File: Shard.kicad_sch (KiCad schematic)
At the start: 27 parts, among them J1 USB_C_Receptacle_USB2.0_16P, J2 Conn_01x02_Pin, U1 ESP32-S3, U2 USBLC6-2P6, U3 TLV76733DRVx, U4 TLV76733DRVx

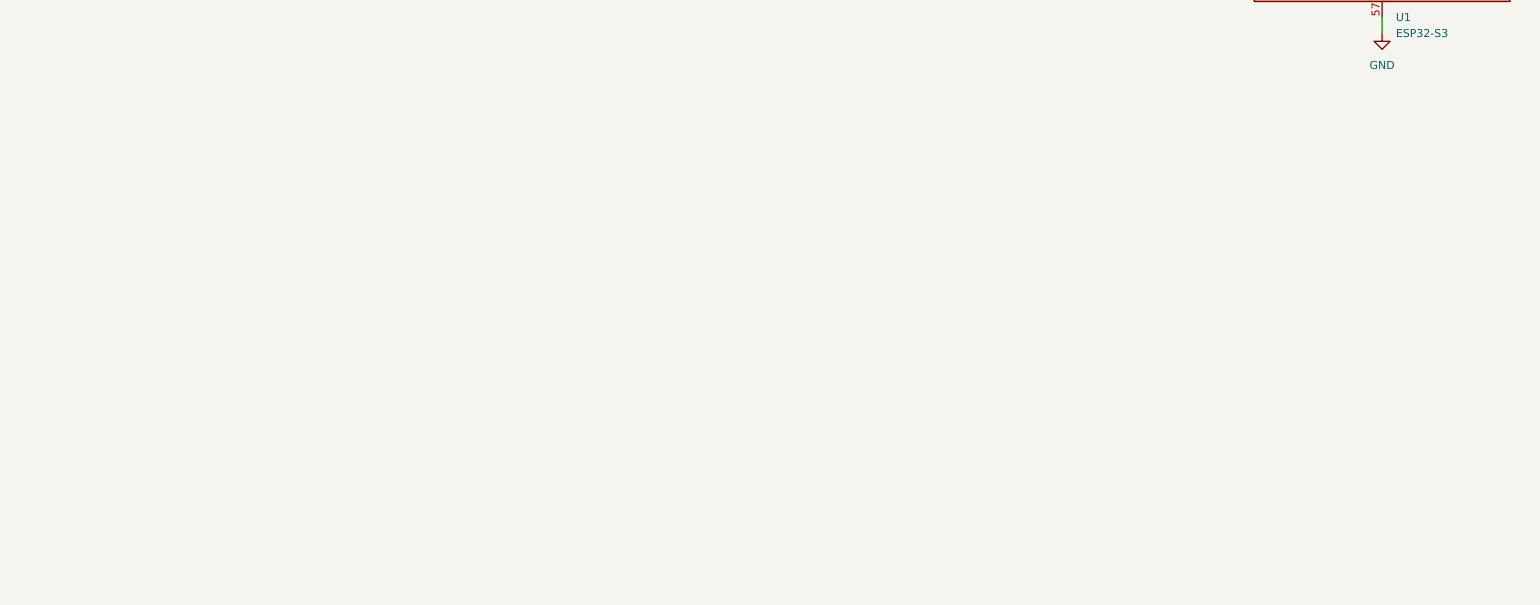
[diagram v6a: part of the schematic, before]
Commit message: Add Reset & boot buttons (footprints and parts associated)
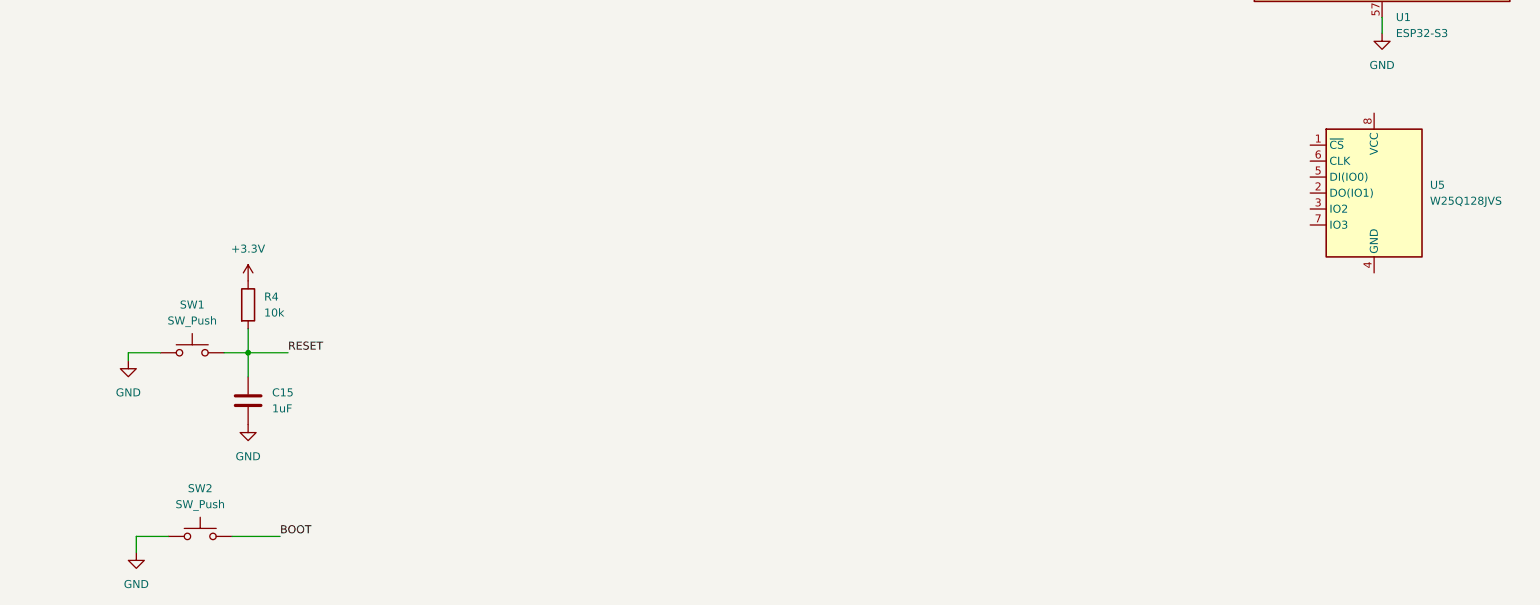
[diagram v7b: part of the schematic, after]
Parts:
- added C15: 1uF, Capacitor_SMD:C_0603_1608Metric, symbol Device:C
- added R4: 10k, Resistor_SMD:R_0402_1005Metric, symbol Device:R
- added SW1, SW2: SW_Push, Button_Switch_SMD:SW_Push_SPST_NO_Alps_SKRK, symbol Switch:SW_Push
- added U5: W25Q128JVS, Package_SO:SOIC-8_5.23x5.23mm_P1.27mm, symbol Memory_Flash:W25Q128JVS
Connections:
- net +3.3V: now also R4.1
- net GND: now also C15.2, SW1.1, SW2.1
- new net BOOT: SW2.2
- new net RESET: C15.1, R4.2, SW1.2

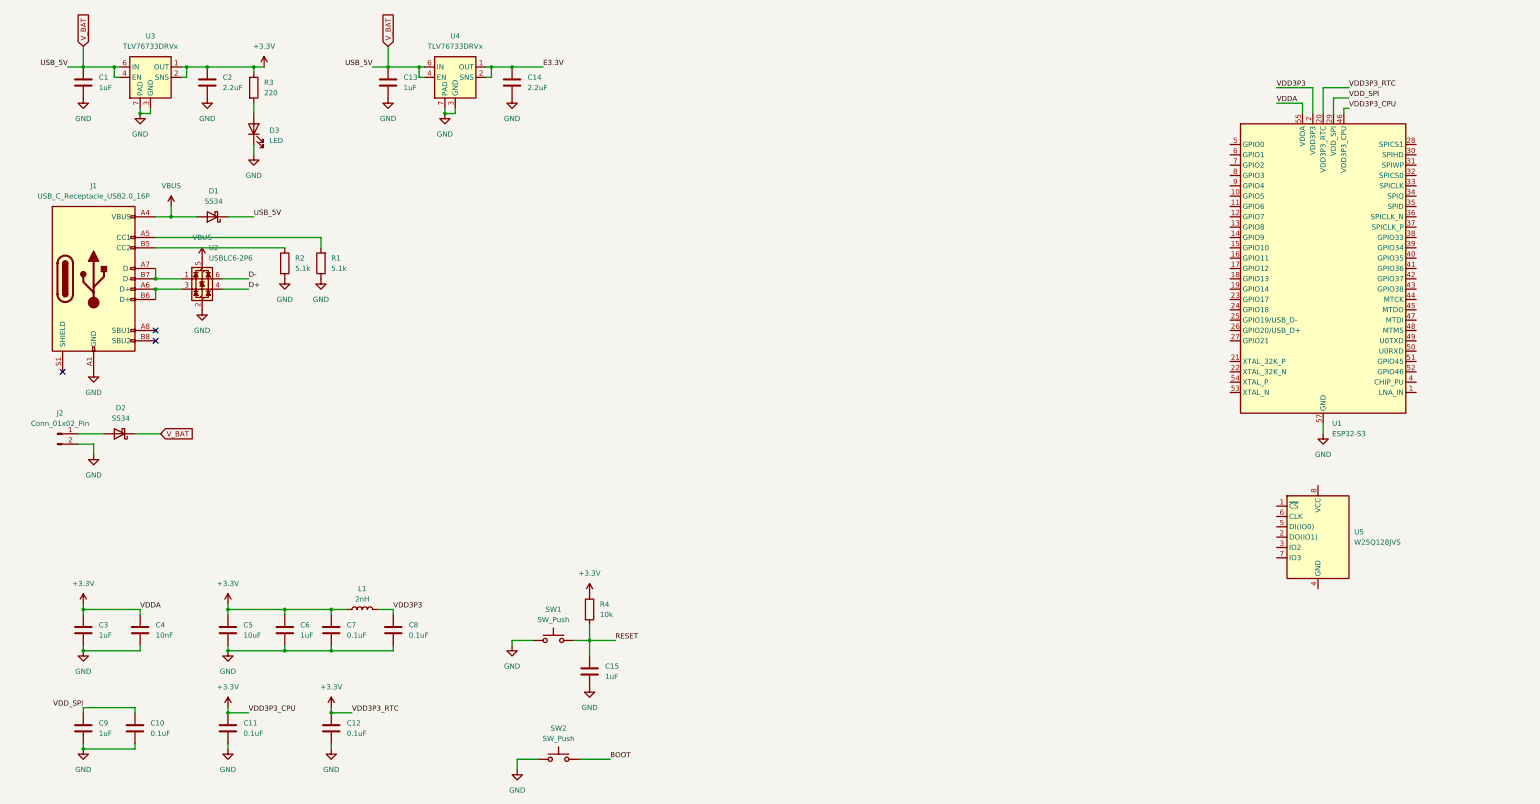
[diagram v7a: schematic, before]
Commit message: Add 16MB Flash with footprint & part
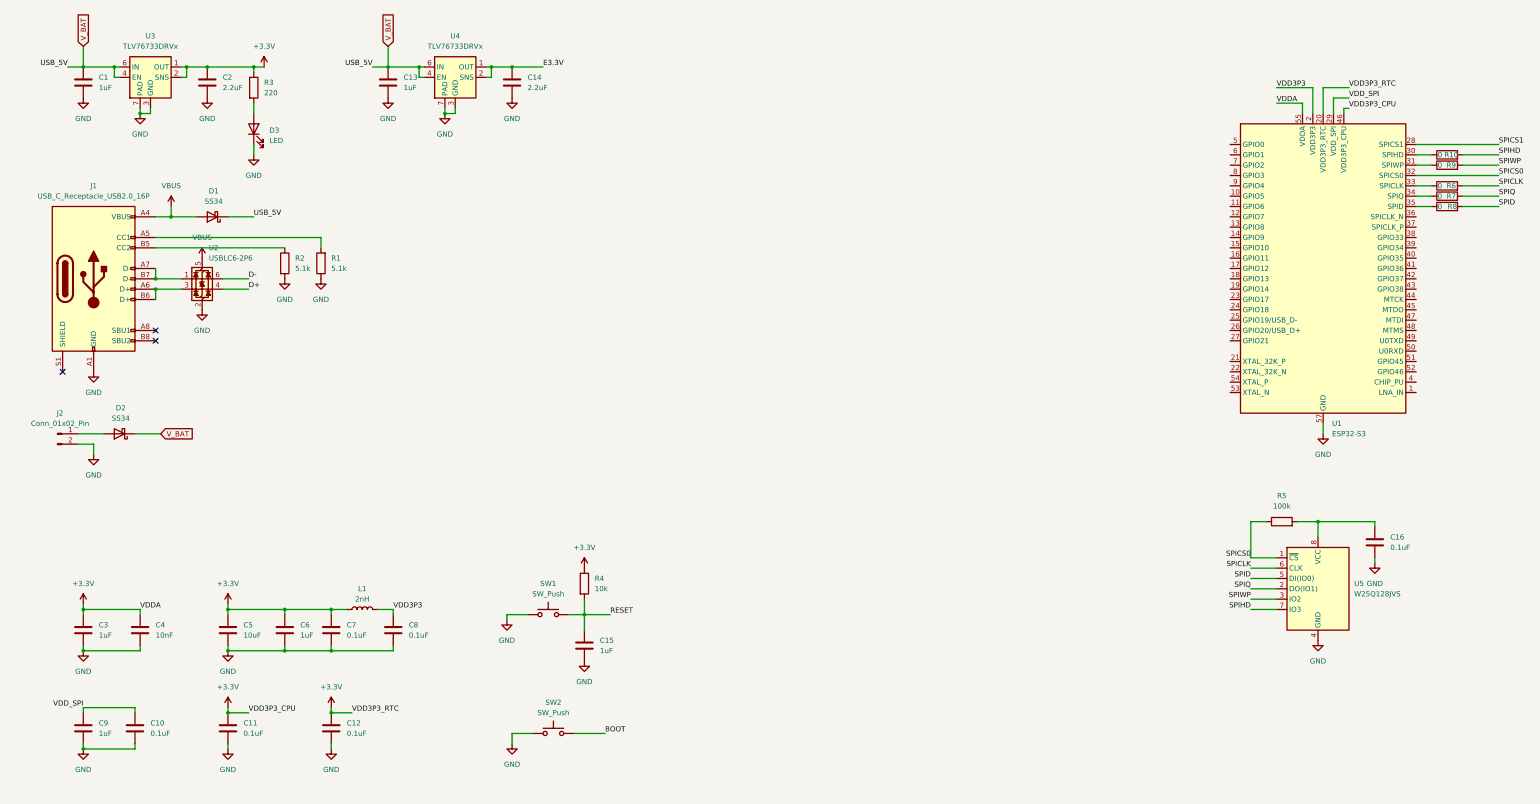
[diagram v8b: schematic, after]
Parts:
- added C16: 0.1uF, Capacitor_SMD:C_1206_3216Metric, symbol Device:C
- added R10, R6, R7, R8, R9: 0, Resistor_SMD:R_0603_1608Metric, symbol Device:R
- added R5: 100k, Resistor_SMD:R_1210_3225Metric, symbol Device:R
- U5: REF (none) -> C97521
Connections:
- net GND: now also U5.4 (GND), C16.2
- net SPICS1: now reaches U1.28 (SPICS1)
- net at U1.30 (SPIHD): now also R10.1
- net at U1.31 (SPIWP): now also R9.1
- net SPICS0: now reaches U1.32 (SPICS0)
- net SPICS0: now also U5.1 (~{CS}), R5.1
- net at U1.33 (SPICLK): now also R6.1
- net at U1.34 (SPIQ): now also R7.1
- net at U1.35 (SPID): now also R8.1
- net SPIQ: now reaches U5.2 (DO(IO1))
- net SPIQ: now also R7.2
- net SPIWP: now reaches U5.3 (IO2)
- net SPIWP: now also R9.2
- net SPID: now reaches U5.5 (DI(IO0))
- net SPID: now also R8.2
- net SPICLK: now reaches U5.6 (CLK)
- net SPICLK: now also R6.2
- net SPIHD: now reaches U5.7 (IO3)
- net SPIHD: now also R10.2
- net at U5.8 (VCC): now also C16.1, R5.2
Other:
- moved on the sheet: C15, R4, SW1, SW2, U5
